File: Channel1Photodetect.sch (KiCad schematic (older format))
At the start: 11 parts, among them P201 CONN_01X01, U201 MCP6404, U202 LM339

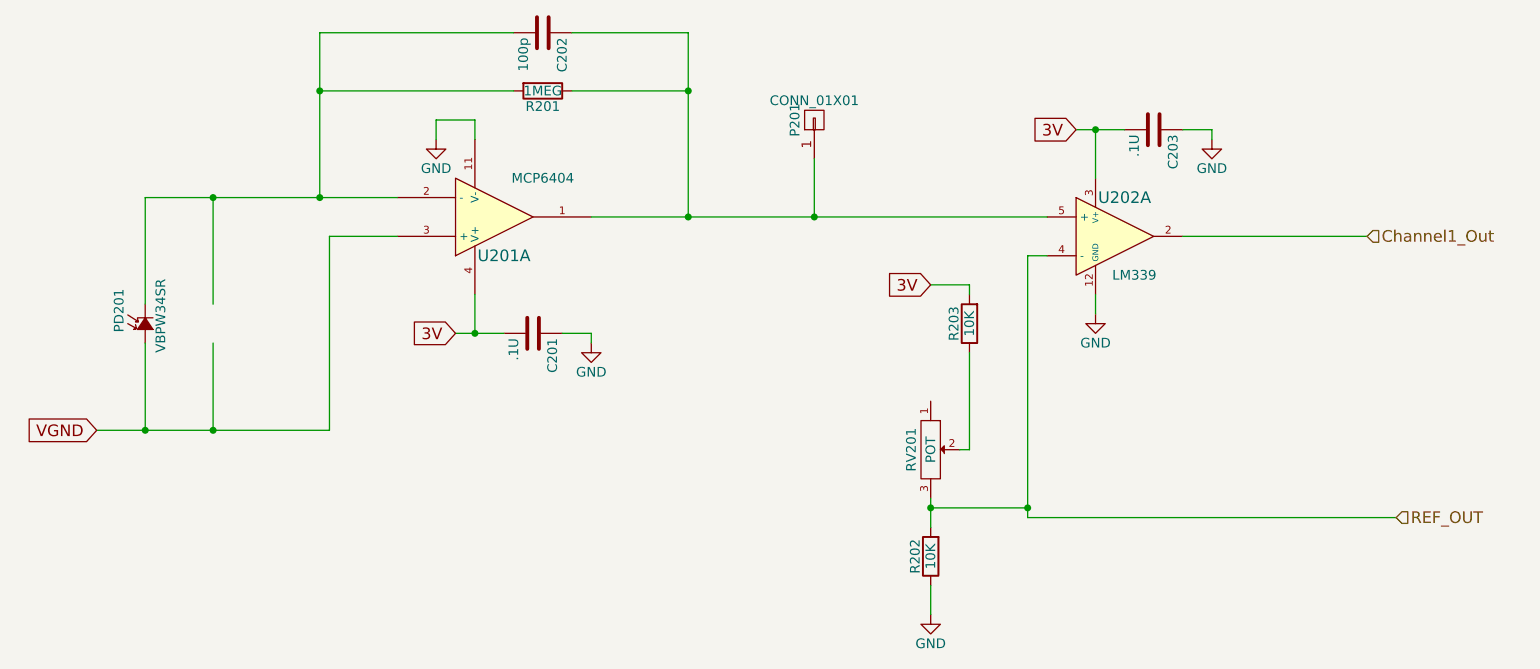
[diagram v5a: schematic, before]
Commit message: Schematic and layout cleanup after photodiode removal
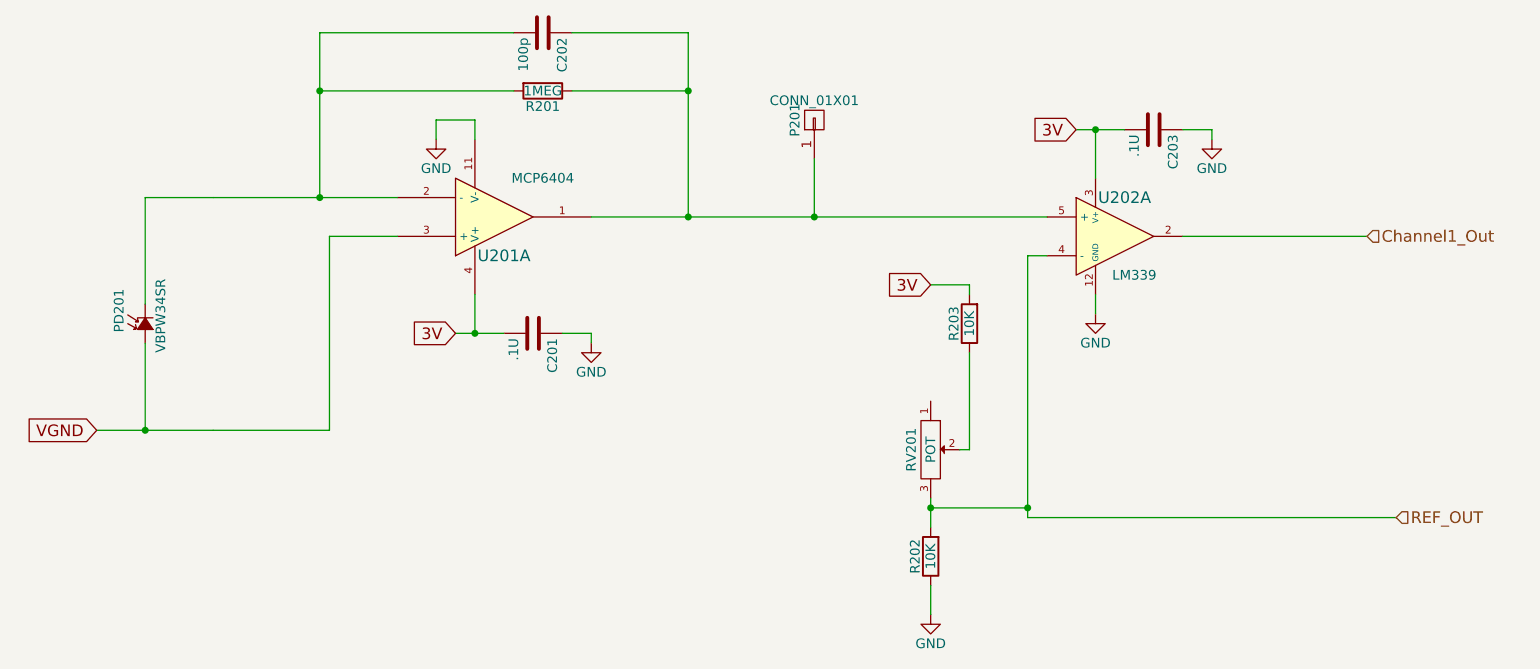
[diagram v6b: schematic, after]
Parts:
- PD201: footprint DasBlinkinput:VPW34SR -> DasBlinkinput:VPW34SR*
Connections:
- wire segments 39 -> 49
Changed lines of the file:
@@
 F 0 "PD201" H 2655 4035 50  0000 L CNN
 F 1 "VBPW34SR" H 2550 3820 50  0000 L CNN
-F 2 "DasBlinkinput:VPW34SR" V 2700 3900 60  0001 C CNN
+F 2 "DasBlinkinput:VPW34SR*" V 2700 3900 60  0001 C CNN
 F 3 "" V 2700 3900 60  0000 C CNN
 F 4 "VBPW34SR" H 2700 3900 60  0001 C CNN "MPN"
@@
 $EndComp
 Wire Wire Line
-	4000 3250 2700 3250
+	4000 3250 3600 3250
+Wire Wire Line
+	3600 3250 3050 3250
+Wire Wire Line
+	3050 3250 2700 3250
 Wire Wire Line
 	2700 3250 2700 3800
 Wire Wire Line
-	3600 2400 3600 3250
+	3600 2400 3600 2700
+Wire Wire Line
+	3600 2700 3600 3250
 Wire Wire Line
 	3600 2700 4600 2700
@@
 	4900 2700 5500 2700
 Wire Wire Line
-	5500 2400 5500 3350
-Wire Wire Line
-	5000 3350 7350 3350
+	5500 2400 5500 2700
+Wire Wire Line
+	5500 2700 5500 3350
+Wire Wire Line
+	5000 3350 5500 3350
+Wire Wire Line
+	5500 3350 6150 3350
+Wire Wire Line
+	6150 3350 7350 3350
 Wire Wire Line
 	4900 2400 5500 2400
@@
 3V
 Wire Wire Line
-	4300 3950 4550 3950
+	4300 3950 4400 3950
+Wire Wire Line
+	4400 3950 4550 3950
 Wire Wire Line
 	4400 3950 4400 3750
@@
 	6950 4550 6900 4550
 Wire Wire Line
-	6750 4800 6750 4950
+	6750 4800 6750 4850
+Wire Wire Line
+	6750 4850 6750 4950
 Wire Wire Line
 	6750 4850 7250 4850
 Wire Wire Line
-	7250 3550 7250 4900
+	7250 3550 7250 4850
+Wire Wire Line
+	7250 4850 7250 4900
 Wire Wire Line
 	7250 3550 7350 3550
@@
 3V
 Wire Wire Line
-	7500 2900 7750 2900
+	7500 2900 7600 2900
+Wire Wire Line
+	7600 2900 7750 2900
 $Comp
 L C C203
@@
 	3650 4450 3650 3450
 Wire Wire Line
-	2450 4450 3650 4450
+	2450 4450 2700 4450
+Wire Wire Line
+	2700 4450 3050 4450
+Wire Wire Line
+	3050 4450 3650 4450
 Wire Wire Line
 	2700 4450 2700 4000
@@
 VGND
 Connection ~ 2700 4450
-Wire Wire Line
-	3050 3800 3050 3250
-Connection ~ 3050 3250
-Wire Wire Line
-	3050 4000 3050 4450
-Connection ~ 3050 4450
 $EndSCHEMATC

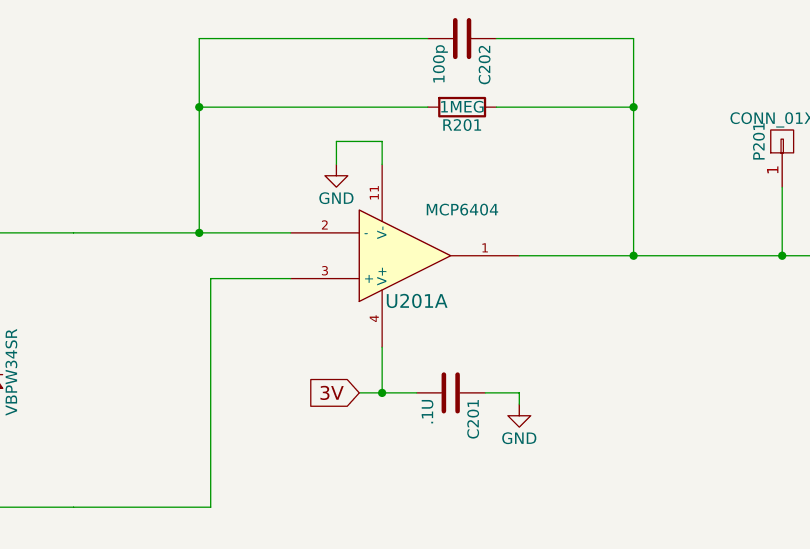
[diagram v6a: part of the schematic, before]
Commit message: Routed all passives related to U201 and the photodiodes
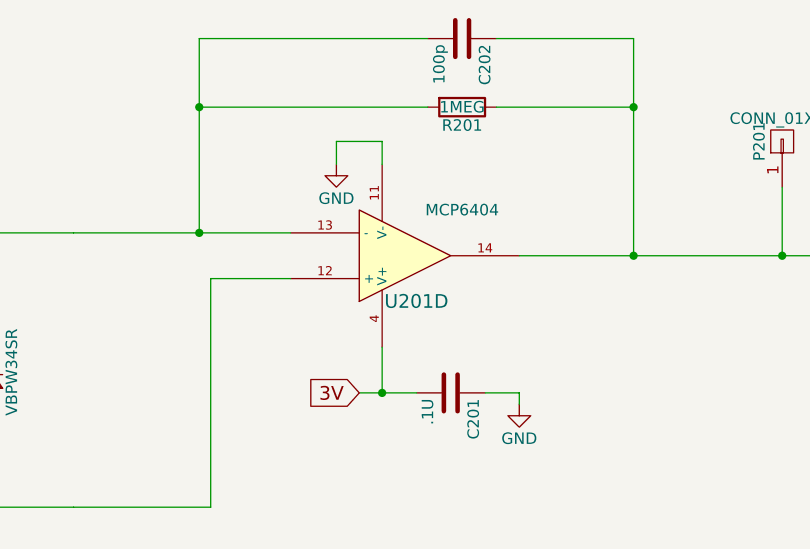
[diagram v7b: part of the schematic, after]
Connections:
- net VGND: now also U201.12 (+); no longer U201.3 (+)
- net at C202.1, P201.1 (P1), R201.1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: now also U201.14; no longer U201.1
- net at C202.2, PD201.2 (C), R201.2: now also U201.13 (-); no longer U201.2 (-)
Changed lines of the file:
@@
 $Comp
 L MCP6404-E/SL U201
-U 1 1 5552D50D
+U 4 1 5552D50D
 P 4500 3350
 F 0 "U201" H 4550 3550 60  0000 C CNN
@@
 F 4 "MCP6404-E/SL" H 4500 3350 60  0001 C CNN "MPN"
 F 5 "http://parts.io/detail/3584122/MCP6404-E%2FSL" H 4500 3350 60  0001 C CNN "Link"
-	1    4500 3350
+	4    4500 3350
 	1    0    0    1
 $EndComp

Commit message: Routed remainder of lines and added test points with lables
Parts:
- RV201: footprint (none) -> Current:P090L-02F25BR10K
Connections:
- net REF_OUT: now also U202.6 (-); no longer U202.4 (-)
- net at C202.1, P201.1 (P1), R201.1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: now also U202.7 (+); no longer U202.5 (+)
- removed net Channel1_Out: U202.2
- new net PD2: U202.1
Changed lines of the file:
@@
 $EndComp
 Wire Wire Line
-	4000 3250 3600 3250
-Wire Wire Line
-	3600 3250 3050 3250
-Wire Wire Line
-	3050 3250 2700 3250
+	2700 3250 4000 3250
 Wire Wire Line
 	2700 3250 2700 3800
 Wire Wire Line
-	3600 2400 3600 2700
-Wire Wire Line
-	3600 2700 3600 3250
+	3600 2400 3600 3250
 Wire Wire Line
 	3600 2700 4600 2700
@@
 	4900 2700 5500 2700
 Wire Wire Line
-	5500 2400 5500 2700
-Wire Wire Line
-	5500 2700 5500 3350
-Wire Wire Line
-	5000 3350 5500 3350
-Wire Wire Line
-	5500 3350 6150 3350
-Wire Wire Line
-	6150 3350 7350 3350
+	5500 2400 5500 3350
+Wire Wire Line
+	5000 3350 7350 3350
 Wire Wire Line
 	4900 2400 5500 2400
@@
 3V
 Wire Wire Line
-	4300 3950 4400 3950
-Wire Wire Line
-	4400 3950 4550 3950
+	4300 3950 4550 3950
 Wire Wire Line
 	4400 3950 4400 3750
@@
 $Comp
 L LM339 U202
-U 1 1 5552D556
+U 2 1 5552D556
 P 7700 3450
 F 0 "U202" H 7750 3650 60  0000 C CNN
@@
 F 4 "LM339DE4" H 7700 3450 60  0001 C CNN "MPN"
 F 5 "http://parts.io/detail/916254/LM339DE4" H 7700 3450 60  0001 C CNN "Link"
-	1    7700 3450
+	2    7700 3450
 	1    0    0    -1
 $EndComp
@@
 F 0 "RV201" H 6750 4450 50  0000 C CNN
 F 1 "POT" H 6750 4550 50  0000 C CNN
-F 2 "" H 6750 4550 60  0001 C CNN
+F 2 "Current:P090L-02F25BR10K" H 6750 4550 60  0001 C CNN
 F 3 "" H 6750 4550 60  0000 C CNN
 F 4 "P090L-02F25BR10K" H 6750 4550 60  0001 C CNN "MPN"
@@
 	6950 4550 6900 4550
 Wire Wire Line
-	6750 4800 6750 4850
-Wire Wire Line
-	6750 4850 6750 4950
+	6750 4800 6750 4950
 Wire Wire Line
 	6750 4850 7250 4850
 Wire Wire Line
-	7250 3550 7250 4850
-Wire Wire Line
-	7250 4850 7250 4900
+	7250 3550 7250 4900
 Wire Wire Line
 	7250 3550 7350 3550
@@
 3V
 Wire Wire Line
-	7500 2900 7600 2900
-Wire Wire Line
-	7600 2900 7750 2900
+	7500 2900 7750 2900
 $Comp
 L C C203
@@
 	7600 3750 7600 3850
 Text HLabel 9000 3450 2    60   Input ~ 0
-Channel1_Out
+PD2
 Text HLabel 9150 4900 2    60   Input ~ 0
 REF_OUT
@@
 	3650 4450 3650 3450
 Wire Wire Line
-	2450 4450 2700 4450
-Wire Wire Line
-	2700 4450 3050 4450
-Wire Wire Line
-	3050 4450 3650 4450
+	2450 4450 3650 4450
 Wire Wire Line
 	2700 4450 2700 4000
